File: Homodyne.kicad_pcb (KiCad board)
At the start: 2 copper layers, 65 x 65 mm, 49 parts, among them J1 5-1814832-1, J4 Conn_01x03_Male 0022232031, U1 LM337_SOT223, U2 LM317DCYR, U3 OPA847xD, U4 LM337_SOT223, U5 LM317DCYR

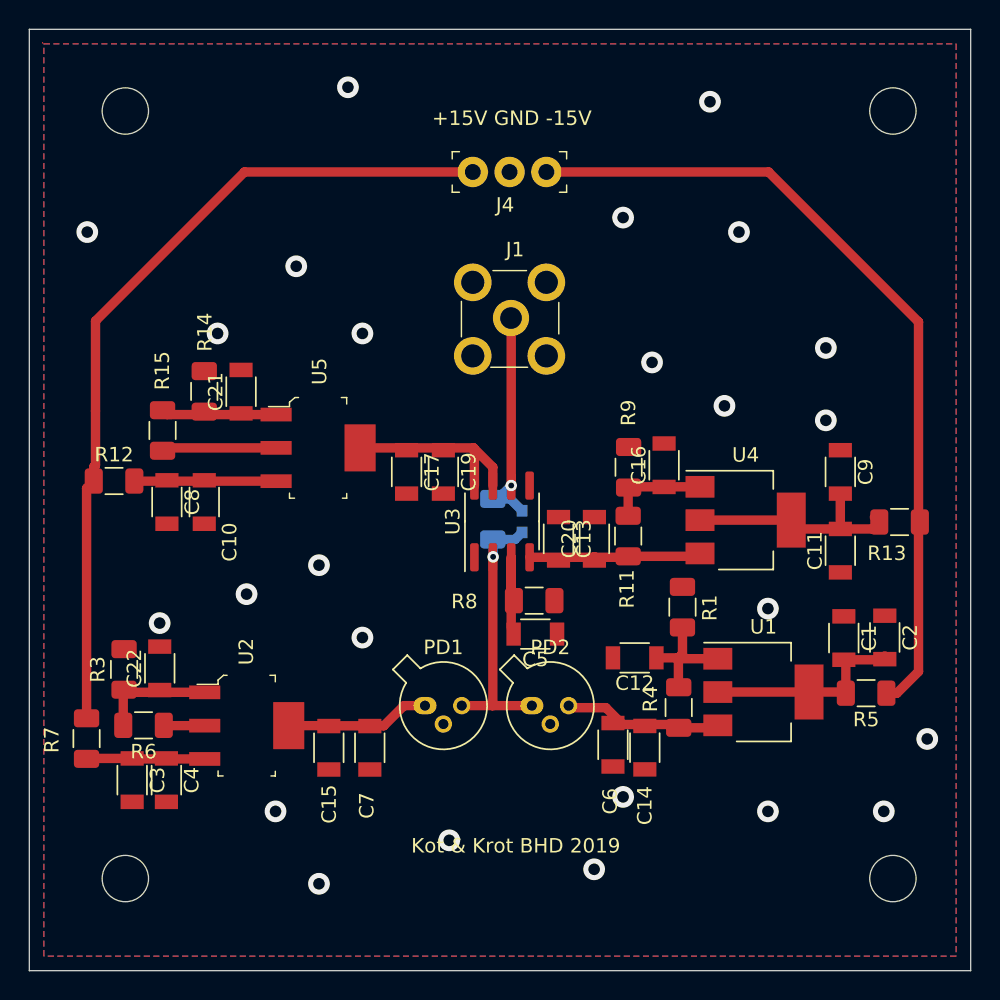
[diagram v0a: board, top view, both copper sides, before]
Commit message: Updated the board size to 65x65 mm
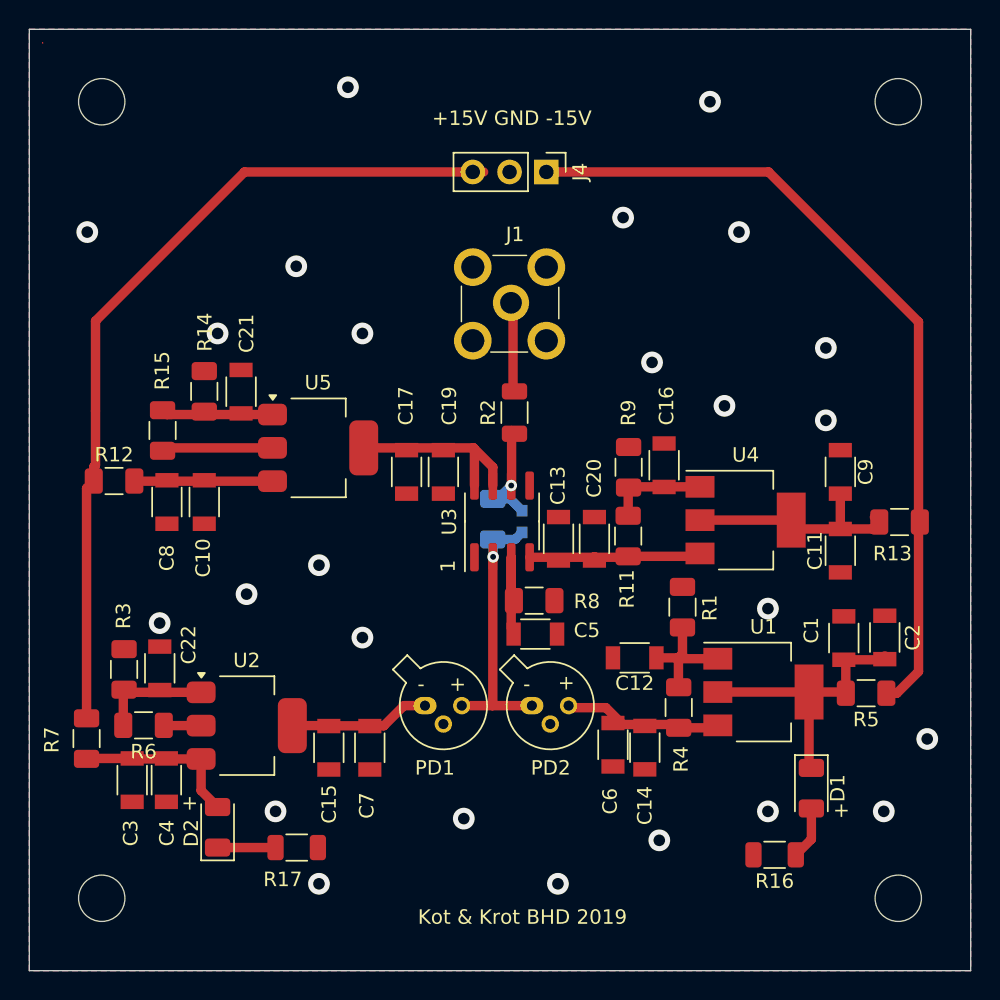
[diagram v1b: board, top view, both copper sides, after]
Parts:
- added D1: LED, LED_SMD:LED_1206_3216Metric, F.Cu at (174.0, 122.4)
- added D2: LED, LED_SMD:LED_1206_3216Metric, F.Cu at (133.0, 125.1)
- added R16: 20kR, Resistor_SMD:R_1206_3216Metric, F.Cu at (171.5, 127.0)
- added R17: 20kR, Resistor_SMD:R_1206_3216Metric, F.Cu at (138.5, 126.5)
- added R2: 0 R, Resistor_SMD:R_1206_3216Metric, F.Cu at (153.5, 96.5)
- J4: footprint digikey-footprints:PinHeader_1x3_P2.54_Drill1.1mm -> Connector_PinHeader_2.54mm:PinHeader_1x03_P2.54mm_Vertical
- U2, U5: footprint digikey-footprints:SOT-223-4 -> Package_TO_SOT_SMD:SOT-223
- moved ? 2.12 mm to (125.0, 130.0)
- moved ? 1.75 mm to (125.0, 75.0)
- moved ? 1.41 mm to (180.0, 130.0)
- moved J1 1.05 mm to (153.2, 89.0)
- moved ? 0.74 mm to (180.0, 75.0)
- turned J4 to -90 degrees
- turned U2 to 0 degrees
- turned U5 to 0 degrees
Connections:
- J1 pad 2: Net-(C18-Pad1) -> Net-(J1-Pad2)
- U3 pad 1: Net-(U3-Pad1) -> unconnected-(U3-NC-Pad1)
- U3 pad 5: Net-(U3-Pad5) -> unconnected-(U3-NC-Pad5)
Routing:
- net Net-(C18-Pad1): track 15.8 -> 4.02 mm
- net Net-(D1-K): track 14.0 -> 19.3 mm
- net Net-(D2-K): track 0.00 -> 4.00 mm
- net Net-(D2-A): track 8.19 -> 12.0 mm
- net Net-(D1-A): track 0.00 -> 3.65 mm
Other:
- rule pad_to_mask_clearance: 0.051 -> 0
- board text added: "+"
- board text added: "-"
- board text added: "1"
